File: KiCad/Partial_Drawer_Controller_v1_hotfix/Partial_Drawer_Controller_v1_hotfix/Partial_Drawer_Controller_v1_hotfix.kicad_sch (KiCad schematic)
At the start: 69 parts, among them J1 Conn_02x03_Odd_Even, J2 Conn_02x04_Odd_Even, J3 Conn_02x05_Odd_Even, U1 PESD2CANFD24L-TR, X1 Conn_01x04_2.5mm_JST_S04B-XAS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, X10 Conn_01x03_3.0mm_Molex_Micro_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, X11 Conn_01x03_3.0mm_Molex_Micro_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, X12 Conn_01x04_2.5mm_JST_S04B-XAS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, X13 Conn_01x03_2.5mm_JST_S04B-XAS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, X2 Conn_01x02_2.5mm_JST_S02B-XAS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

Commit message: chore: updates parts and BOM export for `Partial_Drawer_Controller_v1_hotfix`
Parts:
- F2: path_to_docs (none) -> Circuit_Protection/Fuses/SMD/Littlefuse
- R1, R2, R3: path_to_docs (none) -> Passive_Components/Resistors/UNI-ROYAL
- U1: OC_MOUSER (none) -> 771-PESD2CANFD24L-TR; path_to_docs (none) -> Circuit_Protection/ESD_Protection_Diodes_TVS_Diodes/Nexperia
- X1, X12, X13, X2, X3: path_to_docs (none) -> Connectors/JST/XA_Connector
- X10, X11, X4, X5, X6, X7, X8, X9: OC_MOUSER (none) -> 538-43650-0316; path_to_docs (none) -> Connectors/Molex/Micro-Fit

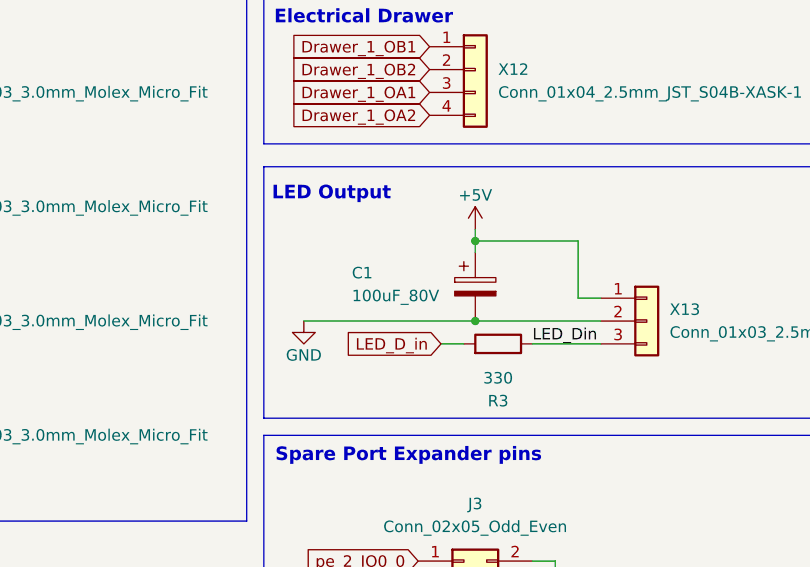
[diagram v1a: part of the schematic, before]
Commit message: chore: updates symbols for `Partial_Drawer_Controller_v1_hotfix` to get docs for every part (not finished yet)
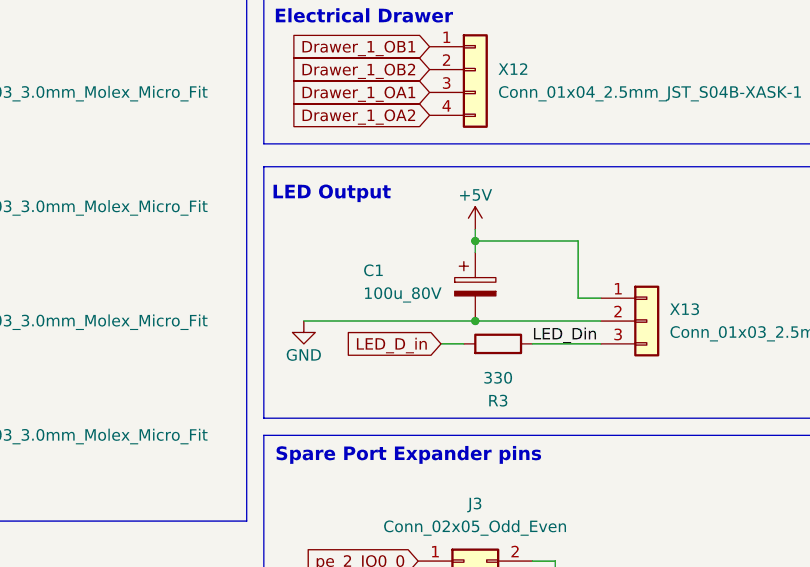
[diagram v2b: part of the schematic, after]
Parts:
- removed C1: 100uF_80V, Capacitor_SMD:CP_Elec_10x10, symbol _C_Polarized:100uF_80V
- added C1: 100u_80V, Capacitor_SMD:CP_Elec_10x10, symbol _C_Polarized:100u_80V
- F1: path_to_docs (none) -> Circuit_Protection/ESD_Protection_Diodes_TVS_Diodes/Liown
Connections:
- net +5V: now also C1.1
- net GND: now also C1.2
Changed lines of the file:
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@@
 	(paper "A3")
 	(junction
+		(at 340.36 105.41)
+		(diameter 0)
+		(color 0 0 0 0)
+	)
+	(junction
 		(at 349.25 134.62)
 		(diameter 0)
@@
 	)
 	(junction
-		(at 340.36 105.41)
-		(diameter 0)
-		(color 0 0 0 0)
-	)
-	(junction
 		(at 31.75 49.53)
 		(diameter 0)
@@
 	(wire
 		(pts
+			(xy 340.36 105.41) (xy 354.33 105.41)
+		)
+		(stroke
+			(width 0)
+			(type default)
+		)
+	)
+	(wire
+		(pts
 			(xy 345.44 36.83) (xy 359.41 36.83)
 		)
@@
 	(wire
 		(pts
-			(xy 340.36 105.41) (xy 354.33 105.41)
-		)
-		(stroke
-			(width 0)
-			(type default)
-		)
-	)
-	(wire
-		(pts
 			(xy 214.63 45.72) (xy 214.63 49.53)
 		)
@@
 	)
 	(symbol
+		(lib_id "_C_Polarized:100u_80V")
+		(at 340.36 101.6 0)
+		(unit 1)
+		(exclude_from_sim no)
+		(in_bom yes)
+		(on_board yes)
+		(dnp no)
+		(property "Reference" "C1"
+			(at 327.914 99.822 0)
+			(effects
+				(font
+					(size 1.27 1.27)
+				)
+				(justify left)
+			)
+		)
+		(property "Value" "100u_80V"
+			(at 327.914 102.362 0)
+			(effects
+				(font
+					(size 1.27 1.27)
+				)
+				(justify left)
+			)
+		)
+		(property "Footprint" "Capacitor_SMD:CP_Elec_10x10"
+			(at 341.3252 105.41 0)
+			(effects
+				(font
+					(size 1.27 1.27)
+				)
+				(hide yes)
+			)
+		)
+		(property "Datasheet" "https://www.mouser.de/datasheet/2/231/161587245243-2307006.pdf"
+			(at 340.36 101.6 0)
+			(effects
+				(font
+					(size 1.27 1.27)
+				)
+				(hide yes)
+			)
+		)
+		(property "Description" "Aluminum Electrolytic Capacitor 100uF 80V ±20% SMD,D10xL10mm"
+			(at 340.36 101.6 0)
+			(effects
+				(font
+					(size 1.27 1.27)
+				)
+				(hide yes)
+			)
+		)
+		(property "MF" "Lelon"
+			(at 340.36 101.6 0)
+			(effects
+				(font
+					(size 1.27 1.27)
+				)
+				(hide yes)
+			)
+		)
+		(property "MPN" "VZH101M1KTR-1010"
+			(at 340.36 101.6 0)
+			(effects
+				(font
+					(size 1.27 1.27)
+				)
+				(hide yes)
+			)
+		)
+		(property "OC_CONRAD" ""
+			(at 340.36 101.6 0)
+			(effects
+				(font
+					(size 1.27 1.27)
+				)
+				(hide yes)
+			)
+		)
+		(property "OC_LCSC" "C249838"
+			(at 340.36 101.6 0)
+			(effects
+				(font
+					(size 1.27 1.27)
+				)
+				(hide yes)
+			)
+		)
+		(property "OC_MOUSER" "140-VZH101M1KTR1010 "
+			(at 340.36 101.6 0)
+			(effects
+				(font
+					(size 1.27 1.27)
+				)
+				(hide yes)
+			)
+		)
+		(property "OC_RS" ""
+			(at 340.36 101.6 0)
+			(effects
+				(font
+					(size 1.27 1.27)
+				)
+				(hide yes)
+			)
+		)
+		(property "path_to_docs" "Passive_Components/Capacitors/Aluminium_Electrolytic_Capacitors/Lelon"
+			(at 340.36 101.6 0)
+			(effects
+				(font
+					(size 1.27 1.27)
+				)
+				(hide yes)
+			)
+		)
+		(pin "1"
+		)
+		(pin "2"
+		)
+		(instances
+			(project ""
+				(path "/57f8c193-fe09-43d3-9441-dbd40881d2aa"
+					(reference "C1")
+					(unit 1)
+				)
+			)
+		)
+	)
+	(symbol
 		(lib_id "Mechanical:MountingHole")
 		(at 342.9 182.88 0)
@@
 			)
 		)
+		(property "OC_CONRAD" ""
+			(at 31.75 55.88 0)
+			(effects
+				(font
+					(size 1.27 1.27)
+				)
+				(hide yes)
+			)
+		)
+		(property "OC_RS" ""
+			(at 31.75 55.88 0)
+			(effects
+				(font
+					(size 1.27 1.27)
+				)
+				(hide yes)
+			)
+		)
+		(property "path_to_docs" "Circuit_Protection/ESD_Protection_Diodes_TVS_Diodes/Liown"
+			(at 31.75 55.88 0)
+			(effects
+				(font
+					(size 1.27 1.27)
+				)
+				(hide yes)
+			)
+		)
 		(pin "2"
 		)
@@
 					(unit 1)
 				)
-			)
-		)
-	)
-	(symbol
-		(lib_id "_C_Polarized:100uF_80V")
-		(at 340.36 101.6 0)
-		(unit 1)
-		(exclude_from_sim no)
-		(in_bom yes)
-		(on_board yes)
-		(dnp no)
-		(property "Reference" "C1"
-			(at 326.644 100.076 0)
-			(effects
-				(font
-					(size 1.27 1.27)
-				)
-				(justify left)
-			)
-		)
-		(property "Value" "100uF_80V"
-			(at 326.644 102.616 0)
-			(effects
-				(font
-					(size 1.27 1.27)
-				)
-				(justify left)
-			)
-		)
-		(property "Footprint" "Capacitor_SMD:CP_Elec_10x10"
-			(at 341.3252 105.41 0)
-			(effects
-				(font
-					(size 1.27 1.27)
-				)
-				(hide yes)
-			)
-		)
-		(property "Datasheet" "https://www.mouser.de/datasheet/2/231/161587245243-2307006.pdf"
-			(at 340.36 101.6 0)
-			(effects
-				(font
-					(size 1.27 1.27)
-				)
-				(hide yes)
-			)
-		)
-		(property "Description" "Aluminum Electrolytic Capacitor 100uF 80V ±20% SMD,D10xL10mm"
-			(at 340.36 101.6 0)
-			(effects
-				(font
-					(size 1.27 1.27)
-				)
-				(hide yes)
-			)
-		)
-		(property "MF" "Lelon"
-			(at 340.36 101.6 0)
-			(effects
-				(font
-					(size 1.27 1.27)
-				)
-				(hide yes)
-			)
-		)
-		(property "MPN" "VZH101M1KTR-1010"
-			(at 340.36 101.6 0)
-			(effects
-				(font
-					(size 1.27 1.27)
-				)
-				(hide yes)
-			)
-		)
-		(property "OC_CONRAD" ""
-			(at 340.36 101.6 0)
-			(effects
-				(font
-					(size 1.27 1.27)
-				)
-				(hide yes)
-			)
-		)
-		(property "OC_LCSC" "C249838"
-			(at 340.36 101.6 0)
-			(effects
-				(font
-					(size 1.27 1.27)
-				)
-				(hide yes)
-			)
-		)
-		(property "OC_MOUSER" "140-VZH101M1KTR1010 "
-			(at 340.36 101.6 0)
-			(effects
-				(font
-					(size 1.27 1.27)
-				)
-				(hide yes)
-			)
-		)
-		(property "OC_RS" ""
-			(at 340.36 101.6 0)
-			(effects
-				(font
-					(size 1.27 1.27)
-				)
-				(hide yes)
-			)
-		)
-		(pin "2"
-		)
-		(pin "1"
-		)
-		(instances
-			(project "Partial_Drawer_Controller_v1"
-				(path "/57f8c193-fe09-43d3-9441-dbd40881d2aa"
-					(reference "C1")
-					(unit 1)
-				)

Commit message: fix: adds `in_bom` attribute for molex connector on `Partial_Drawer_Controller_v1_hotfix`
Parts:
- X10, X11, X4, X5, X6, X7, X8, X9: now in the parts list
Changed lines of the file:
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@@
 		(unit 1)
 		(exclude_from_sim no)
-		(in_bom no)
+		(in_bom yes)
 		(on_board yes)
 		(dnp no)
@@
 		(unit 1)
 		(exclude_from_sim no)
-		(in_bom no)
+		(in_bom yes)
 		(on_board yes)
 		(dnp no)
@@
 		(unit 1)
 		(exclude_from_sim no)
-		(in_bom no)
+		(in_bom yes)
 		(on_board yes)
 		(dnp no)
@@
 		(unit 1)
 		(exclude_from_sim no)
-		(in_bom no)
+		(in_bom yes)
 		(on_board yes)
 		(dnp no)
@@
 		(unit 1)
 		(exclude_from_sim no)
-		(in_bom no)
+		(in_bom yes)
 		(on_board yes)
 		(dnp no)
@@
 		(unit 1)
 		(exclude_from_sim no)
-		(in_bom no)
+		(in_bom yes)
 		(on_board yes)
 		(dnp no)
@@
 		(unit 1)
 		(exclude_from_sim no)
-		(in_bom no)
+		(in_bom yes)
 		(on_board yes)
 		(dnp no)
@@
 		(unit 1)
 		(exclude_from_sim no)
-		(in_bom no)
+		(in_bom yes)
 		(on_board yes)
 		(dnp no)

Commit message: feat: adds `durability` attribute to `Partial_Drawer_Controller_v1_hotfix`
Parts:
- C1: durability (none) -> 5000h@105°C
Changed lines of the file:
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@@
+			)
+		)
+		(property "durability" "5000h@105°C"
+			(at 340.36 101.6 0)
+			(effects
+				(font
+					(size 1.27 1.27)
+				)
+				(hide yes)
 			)
 		)

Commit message: feat: adds more `durability`attributes
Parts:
- X10, X11, X4, X5, X6, X7, X8, X9: durability (none) -> 30 mating cycles
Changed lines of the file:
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@@
 			)
 		)
+		(property "durability" "30 mating cycles"
+			(at 275.59 43.18 0)
+			(effects
+				(font
+					(size 1.27 1.27)
+				)
+				(hide yes)
+			)
+		)
 		(pin "2"
 		)
@@
 			)
 		)
+		(property "durability" "30 mating cycles"
+			(at 275.59 68.58 0)
+			(effects
+				(font
+					(size 1.27 1.27)
+				)
+				(hide yes)
+			)
+		)
 		(pin "2"
 		)
@@
 			)
 		)
+		(property "durability" "30 mating cycles"
+			(at 275.59 106.68 0)
+			(effects
+				(font
+					(size 1.27 1.27)
+				)
+				(hide yes)
+			)
+		)
 		(pin "2"
 		)
@@
 			)
 		)
+		(property "durability" "30 mating cycles"
+			(at 275.59 93.98 0)
+			(effects
+				(font
+					(size 1.27 1.27)
+				)
+				(hide yes)
+			)
+		)
 		(pin "2"
 		)
@@
 			)
 		)
+		(property "durability" "30 mating cycles"
+			(at 275.59 81.28 0)
+			(effects
+				(font
+					(size 1.27 1.27)
+				)
+				(hide yes)
+			)
+		)
 		(pin "2"
 		)
@@
 			)
 		)
+		(property "durability" "30 mating cycles"
+			(at 275.59 55.88 0)
+			(effects
+				(font
+					(size 1.27 1.27)
+				)
+				(hide yes)
+			)
+		)
 		(pin "2"
 		)
@@
 			)
 		)
+		(property "durability" "30 mating cycles"
+			(at 275.59 30.48 0)
+			(effects
+				(font
+					(size 1.27 1.27)
+				)
+				(hide yes)
+			)
+		)
 		(pin "2"
 		)
@@
 			(at 275.59 119.38 0)
 			(effects
+				(font
+					(size 1.27 1.27)
+				)
+				(hide yes)
+			)
+		)
+		(property "durability" "30 mating cycles"
+			(at 275.59 119.38 0)
+			(effects

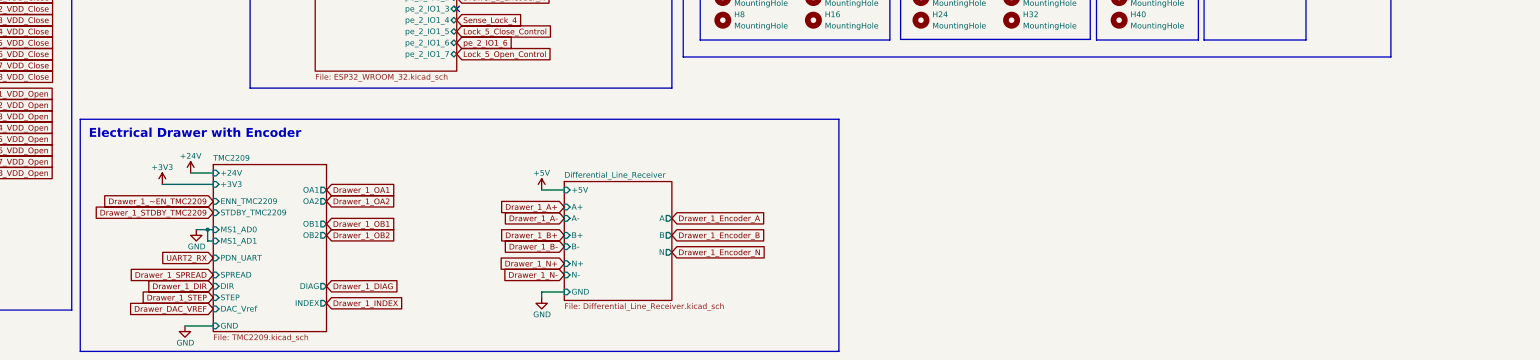
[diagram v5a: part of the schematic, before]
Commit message: docs: adds important hint for flashing the ESP's
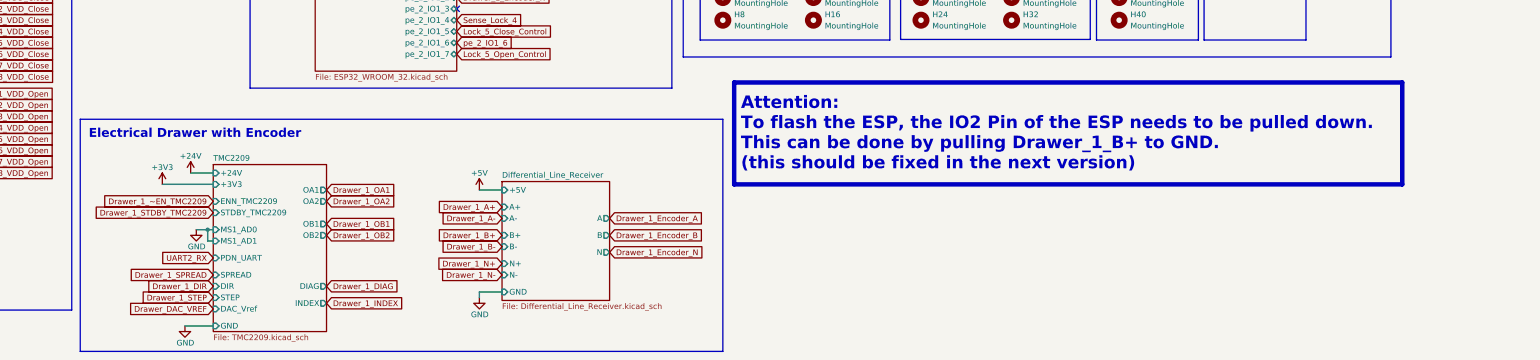
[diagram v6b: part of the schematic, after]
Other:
- note added: "Attention: To flash the ESP, the IO2 Pin of the ESP needs to be pulled down. This can be done by pulling Drawer_1_B+ to GND. (this should be fixed in the next version)"
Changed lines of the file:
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@@
 	(wire
 		(pts
-			(xy 213.36 269.24) (xy 213.36 270.51)
+			(xy 199.39 269.24) (xy 199.39 270.51)
 		)
 		(stroke
@@
 	(wire
 		(pts
-			(xy 218.44 269.24) (xy 213.36 269.24)
+			(xy 204.47 269.24) (xy 199.39 269.24)
 		)
 		(stroke
@@
 	(wire
 		(pts
-			(xy 213.36 246.38) (xy 218.44 246.38)
+			(xy 199.39 246.38) (xy 204.47 246.38)
 		)
 		(stroke
@@
 	)
 	(rectangle
+		(start 256.54 222.25)
+		(end 406.4 245.11)
+		(stroke
+			(width 1)
+			(type default)
+			(color 255 0 0 1)
+		)
+		(fill
+			(type none)
+		)
+	)
+	(rectangle
 		(start 15.875 21.59)
 		(end 78.74 36.195)
@@
 	(rectangle
 		(start 109.855 230.505)
-		(end 280.035 282.575)
+		(end 254 282.575)
 		(stroke
 			(width 0)
@@
 		)
 	)
+	(text "Attention:\nTo flash the ESP, the IO2 Pin of the ESP needs to be pulled down.\nThis can be done by pulling Drawer_1_B+ to GND.\n(this should be fixed in the next version)"
+		(exclude_from_sim no)
+		(at 258.064 233.68 0)
+		(effects
+			(font
+				(size 2.8 2.8)
+				(thickness 0.6)
+				(bold yes)
+				(color 255 0 0 1)
+			)
+			(justify left)
+		)
+	)
 	(text "CAN and Power Input"
 		(exclude_from_sim no)
@@
 	(global_label "Drawer_1_Encoder_N"
 		(shape input)
-		(at 242.57 260.35 0)
+		(at 228.6 260.35 0)
 		(fields_autoplaced yes)
 		(effects
@@
 		)
 		(property "Intersheetrefs" "${INTERSHEET_REFS}"
-			(at 264.8885 260.35 0)
+			(at 250.9185 260.35 0)
 			(effects
 				(font
@@
 	(global_label "Drawer_1_B+"
 		(shape input)
-		(at 218.44 256.54 180)
+		(at 204.47 256.54 180)
 		(fields_autoplaced yes)
 		(effects
@@
 		)
 		(property "Intersheetrefs" "${INTERSHEET_REFS}"
-			(at 203.1366 256.54 0)
+			(at 189.1666 256.54 0)
 			(effects
 				(font
@@
 	(global_label "Drawer_1_N+"
 		(shape input)
-		(at 218.44 262.89 180)
+		(at 204.47 262.89 180)
 		(fields_autoplaced yes)
 		(effects
@@
 		)
 		(property "Intersheetrefs" "${INTERSHEET_REFS}"
-			(at 203.0761 262.89 0)
+			(at 189.1061 262.89 0)
 			(effects
 				(font
@@
 	(global_label "Drawer_1_Encoder_B"
 		(shape input)
-		(at 242.57 256.54 0)
+		(at 228.6 256.54 0)
 		(fields_autoplaced yes)
 		(effects
@@
 		)
 		(property "Intersheetrefs" "${INTERSHEET_REFS}"
-			(at 264.828 256.54 0)
+			(at 250.858 256.54 0)
 			(effects
 				(font
@@
 	(global_label "Drawer_1_N-"
 		(shape input)
-		(at 218.44 265.43 180)
+		(at 204.47 265.43 180)
 		(fields_autoplaced yes)
 		(effects
@@
 		)
 		(property "Intersheetrefs" "${INTERSHEET_REFS}"
-			(at 203.0761 265.43 0)
+			(at 189.1061 265.43 0)
 			(effects
 				(font
@@
 	(global_label "Drawer_1_A-"
 		(shape input)
-		(at 218.44 252.73 180)
+		(at 204.47 252.73 180)
 		(fields_autoplaced yes)
 		(effects
@@
 		)
 		(property "Intersheetrefs" "${INTERSHEET_REFS}"
-			(at 203.318 252.73 0)
+			(at 189.348 252.73 0)
 			(effects
 				(font
@@
 	(global_label "Drawer_1_Encoder_A"
 		(shape input)
-		(at 242.57 252.73 0)
+		(at 228.6 252.73 0)
 		(fields_autoplaced yes)
 		(effects
@@
 		)
 		(property "Intersheetrefs" "${INTERSHEET_REFS}"
-			(at 264.6466 252.73 0)
+			(at 250.6766 252.73 0)
 			(effects
 				(font
@@
 	(global_label "Drawer_1_B-"
 		(shape input)
-		(at 218.44 259.08 180)
+		(at 204.47 259.08 180)
 		(fields_autoplaced yes)
 		(effects
@@
 		)
 		(property "Intersheetrefs" "${INTERSHEET_REFS}"
-			(at 203.1366 259.08 0)
+			(at 189.1666 259.08 0)
 			(effects
 				(font
@@
 	(global_label "Drawer_1_A+"
 		(shape input)
-		(at 218.44 250.19 180)
+		(at 204.47 250.19 180)
 		(fields_autoplaced yes)
 		(effects
@@
 		)
 		(property "Intersheetrefs" "${INTERSHEET_REFS}"
-			(at 203.318 250.19 0)
+			(at 189.348 250.19 0)
 			(effects
 				(font
@@
 	(symbol
 		(lib_id "power:GND")
-		(at 213.36 270.51 0)
+		(at 199.39 270.51 0)
 		(unit 1)
 		(exclude_from_sim no)
@@
 		(dnp no)
 		(property "Reference" "#PWR026"
-			(at 213.36 276.86 0)
+			(at 199.39 276.86 0)
 			(effects
 				(font
@@
 		)
 		(property "Value" "GND"
-			(at 211.455 274.32 0)
+			(at 197.485 274.32 0)
 			(effects
 				(font
@@
 		)
 		(property "Footprint" ""
-			(at 213.36 270.51 0)
+			(at 199.39 270.51 0)
 			(effects
 				(font
@@
 		)
 		(property "Datasheet" ""
-			(at 213.36 270.51 0)
+			(at 199.39 270.51 0)
 			(effects
 				(font
@@
 		)
 		(property "Description" "Power symbol creates a global label with name \"GND\" , ground"
-			(at 213.36 270.51 0)
+			(at 199.39 270.51 0)
 			(effects
 				(font
@@
 	(symbol
 		(lib_id "power:+5V")
-		(at 213.36 246.38 0)
+		(at 199.39 246.38 0)
 		(unit 1)
 		(exclude_from_sim no)
@@
 		(dnp no)
 		(property "Reference" "#PWR025"
-			(at 213.36 250.19 0)
+			(at 199.39 250.19 0)
 			(effects
 				(font
@@
 		)
 		(property "Value" "+5V"
-			(at 213.36 242.57 0)
+			(at 199.39 242.57 0)
 			(effects
 				(font
@@
 		)
 		(property "Footprint" ""
-			(at 213.36 246.38 0)
+			(at 199.39 246.38 0)
 			(effects
 				(font
@@
 		)
 		(property "Datasheet" ""
-			(at 213.36 246.38 0)
+			(at 199.39 246.38 0)
 			(effects
 				(font
@@
 		)
 		(property "Description" "Power symbol creates a global label with name \"+5V\""
-			(at 213.36 246.38 0)
+			(at 199.39 246.38 0)
 			(effects
 				(font
@@
 	)
 	(sheet
-		(at 218.44 244.475)
+		(at 204.47 244.475)
 		(size 24.13 26.67)
 		(fields_autoplaced yes)
@@
 		)
 		(property "Sheetname" "Differential_Line_Receiver"
-			(at 218.44 243.7634 0)
+			(at 204.47 243.7634 0)
 			(effects
 				(font
@@
 		)
 		(property "Sheetfile" "Differential_Line_Receiver.kicad_sch"
-			(at 218.44 271.7296 0)
+			(at 204.47 271.7296 0)
 			(effects
 				(font
@@
 		)
 		(pin "A+" input
-			(at 218.44 250.19 180)
+			(at 204.47 250.19 180)
 			(effects
 				(font
@@
 		)
 		(pin "+5V" input
-			(at 218.44 246.38 180)
+			(at 204.47 246.38 180)
 			(effects
 				(font
@@
 		)
 		(pin "A-" input
-			(at 218.44 252.73 180)
+			(at 204.47 252.73 180)
 			(effects
 				(font
@@
 		)
 		(pin "B-" input
-			(at 218.44 259.08 180)
+			(at 204.47 259.08 180)
 			(effects
 				(font
@@
 		)
 		(pin "N+" input
-			(at 218.44 262.89 180)
+			(at 204.47 262.89 180)
 			(effects
 				(font
@@
 		)
 		(pin "GND" input
-			(at 218.44 269.24 180)
+			(at 204.47 269.24 180)
 			(effects
 				(font
@@
 		)
 		(pin "N-" input
-			(at 218.44 265.43 180)
+			(at 204.47 265.43 180)
 			(effects
 				(font
@@
 		)
 		(pin "B+" input
-			(at 218.44 256.54 180)
+			(at 204.47 256.54 180)
 			(effects
 				(font
@@
 		)
 		(pin "A" output
-			(at 242.57 252.73 0)
+			(at 228.6 252.73 0)
 			(effects
 				(font
@@
 		)
 		(pin "B" output
-			(at 242.57 256.54 0)
+			(at 228.6 256.54 0)
 			(effects
 				(font
@@
 		)
 		(pin "N" output
-			(at 242.57 260.35 0)
+			(at 228.6 260.35 0)
 			(effects
 				(font
